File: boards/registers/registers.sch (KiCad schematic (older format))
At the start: 44 parts, among them U1 SN74LV08APW, U2 MC74HC244ADT, U3 MC74HC273ADT, U4 74HC161PW

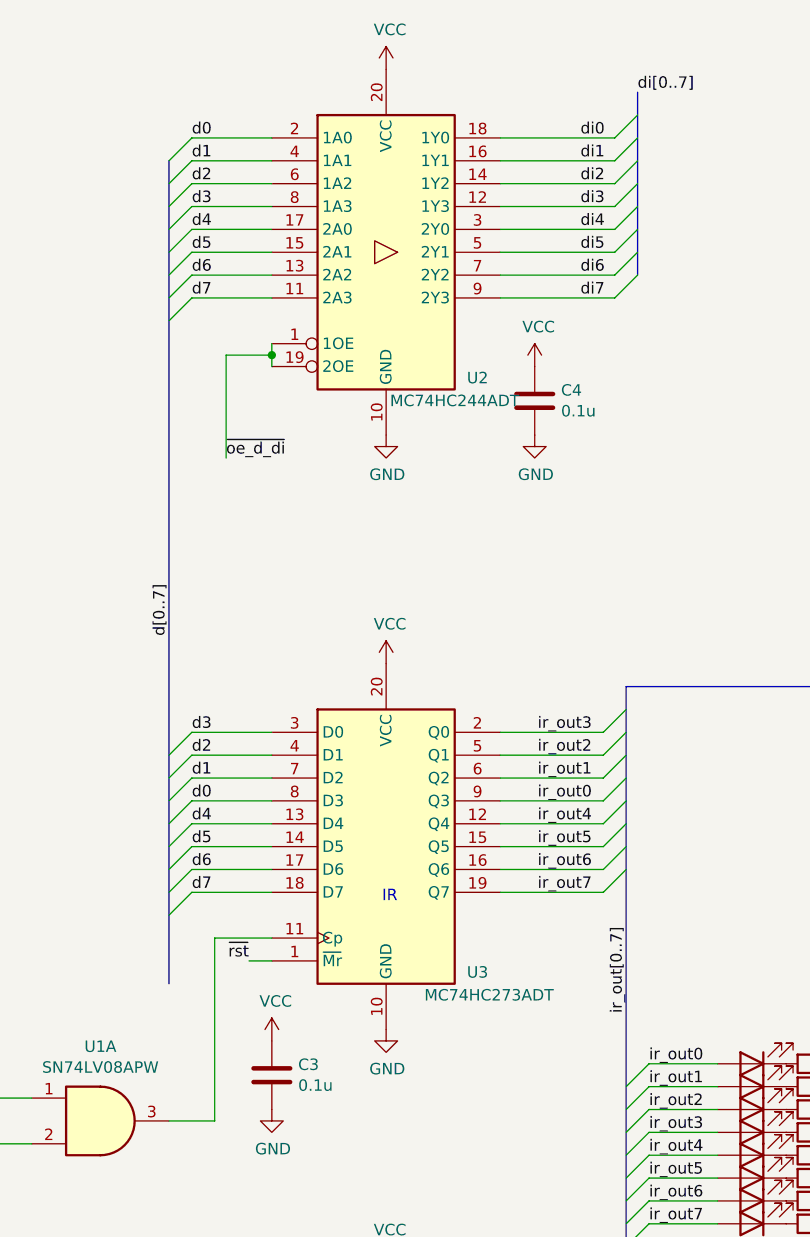
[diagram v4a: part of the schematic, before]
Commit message: Registers board rev. 2
Implement RDY mechanism by suspending clock signal
Take caution against crosstalk on sensitive line
Add proper decoupling capacitors
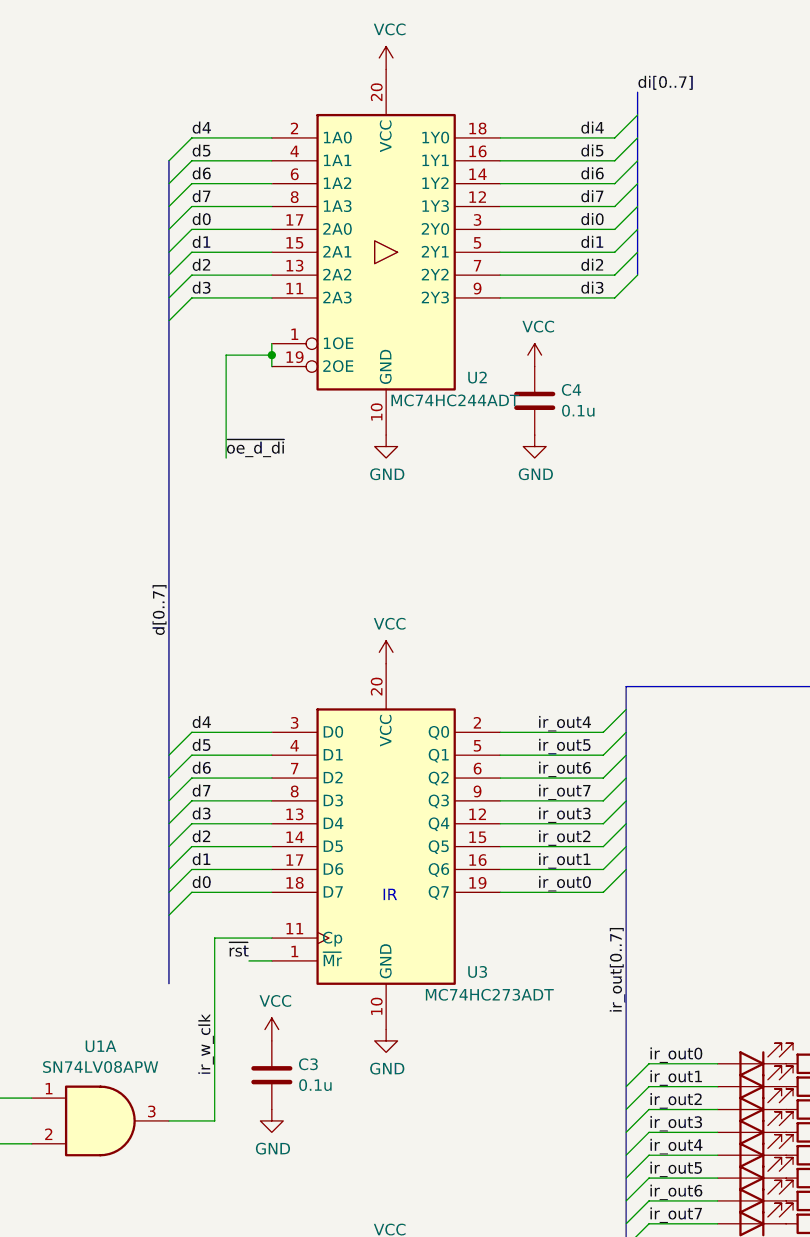
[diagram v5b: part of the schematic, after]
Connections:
- net alu_invert: now also U3.15 (Q5); no longer U3.5 (Q1)
- net alu_op0: now also U3.12 (Q4); no longer U3.2 (Q0)
- net alu_op1: now also U3.2 (Q0); no longer U3.12 (Q4)
- net alu_op2: now also U3.5 (Q1); no longer U3.15 (Q5)
- net alu_op3: now also U3.6 (Q2); no longer U3.16 (Q6)
- net d0: now also U2.17 (2A0), U3.18 (D7); no longer U2.2 (1A0), U3.8 (D3)
- net d1: now also U2.15 (2A1), U3.17 (D6); no longer U2.4 (1A1), U3.7 (D2)
- net d2: now also U2.13 (2A2), U3.14 (D5); no longer U2.6 (1A2), U3.4 (D1)
- net d3: now also U2.11 (2A3), U3.13 (D4); no longer U2.8 (1A3), U3.3 (D0)
- net d4: now also U2.2 (1A0), U3.3 (D0); no longer U2.17 (2A0), U3.13 (D4)
- net d5: now also U2.4 (1A1), U3.4 (D1); no longer U2.15 (2A1), U3.14 (D5)
- net d6: now also U2.6 (1A2), U3.7 (D2); no longer U2.13 (2A2), U3.17 (D6)
- net d7: now also U2.8 (1A3), U3.8 (D3); no longer U2.11 (2A3), U3.18 (D7)
- net di0: now also U2.3 (2Y0); no longer U2.18 (1Y0)
- net di1: now also U2.5 (2Y1); no longer U2.16 (1Y1)
- net di2: now also U2.7 (2Y2); no longer U2.14 (1Y2)
- net di3: now also U2.9 (2Y3); no longer U2.12 (1Y3)
- net di4: now also U2.18 (1Y0); no longer U2.3 (2Y0)
- net di5: now also U2.16 (1Y1); no longer U2.5 (2Y1)
- net di6: now also U2.14 (1Y2); no longer U2.7 (2Y2)
- net di7: now also U2.12 (1Y3); no longer U2.9 (2Y3)
- net ir_out0: now also U3.19 (Q7); no longer U3.9 (Q3)
- net ir_out1: now also U3.16 (Q6); no longer U3.6 (Q2)
- net ir_out7: now also U3.9 (Q3); no longer U3.19 (Q7)
- net ir_w_clk: now reaches U1.3, U3.11 (Cp)
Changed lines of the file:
@@
 ir_out[0..7]
 Wire Wire Line
+	3850 4050 4300 4050
+Wire Wire Line
+	3850 4150 4300 4150
+Wire Wire Line
+	3850 4250 4300 4250
+Wire Wire Line
+	3850 4350 4300 4350
+Wire Wire Line
 	3850 3650 4300 3650
 Wire Wire Line
@@
 Wire Wire Line
 	3850 3950 4300 3950
-Wire Wire Line
-	3850 4050 4300 4050
-Wire Wire Line
-	3850 4150 4300 4150
-Wire Wire Line
-	3850 4250 4300 4250
-Wire Wire Line
-	3850 4350 4300 4350
+Text Label 4250 4050 2    50   ~ 0
+ir_out3
+Text Label 4250 4150 2    50   ~ 0
+ir_out2
+Text Label 4250 4250 2    50   ~ 0
+ir_out1
+Text Label 4250 4350 2    50   ~ 0
+ir_out0
 Text Label 4250 3650 2    50   ~ 0
-ir_out3
+ir_out4
 Text Label 4250 3750 2    50   ~ 0
-ir_out2
+ir_out5
 Text Label 4250 3850 2    50   ~ 0
-ir_out1
+ir_out6
 Text Label 4250 3950 2    50   ~ 0
-ir_out0
-Text Label 4250 4050 2    50   ~ 0
-ir_out4
-Text Label 4250 4150 2    50   ~ 0
-ir_out5
-Text Label 4250 4250 2    50   ~ 0
-ir_out6
-Text Label 4250 4350 2    50   ~ 0
 ir_out7
 Entry Wire Line
@@
 ~clk
 Entry Wire Line
+	2400 1550 2500 1450
+Entry Wire Line
+	2400 1650 2500 1550
+Entry Wire Line
+	2400 1750 2500 1650
+Entry Wire Line
+	2400 1850 2500 1750
+Entry Wire Line
 	2400 1150 2500 1050
 Entry Wire Line
@@
 	2400 1450 2500 1350
 Entry Wire Line
-	2400 1550 2500 1450
-Entry Wire Line
-	2400 1650 2500 1550
-Entry Wire Line
-	2400 1750 2500 1650
-Entry Wire Line
-	2400 1850 2500 1750
-Entry Wire Line
 	2400 3750 2500 3650
 Entry Wire Line
@@
 	2400 4450 2500 4350
 Wire Wire Line
+	2850 3950 2500 3950
+Wire Wire Line
+	2500 3850 2850 3850
+Wire Wire Line
+	2850 3750 2500 3750
+Wire Wire Line
+	2500 3650 2850 3650
+Wire Wire Line
 	2850 4350 2500 4350
 Wire Wire Line
@@
 	2500 4050 2850 4050
 Wire Wire Line
-	2850 3950 2500 3950
-Wire Wire Line
-	2500 3850 2850 3850
-Wire Wire Line
-	2850 3750 2500 3750
-Wire Wire Line
-	2500 3650 2850 3650
+	2500 1450 2850 1450
+Wire Wire Line
+	2850 1550 2500 1550
+Wire Wire Line
+	2500 1650 2850 1650
+Wire Wire Line
+	2850 1750 2500 1750
 Wire Wire Line
 	2500 1050 2850 1050
@@
 Wire Wire Line
 	2850 1350 2500 1350
-Wire Wire Line
-	2500 1450 2850 1450
-Wire Wire Line
-	2850 1550 2500 1550
-Wire Wire Line
-	2500 1650 2850 1650
-Wire Wire Line
-	2850 1750 2500 1750
 Wire Wire Line
 	2850 1950 2850 2000
 Text Label 2400 3000 3    50   ~ 0
 d[0..7]
+Text Label 2500 1450 0    50   ~ 0
+d0
+Text Label 2500 1550 0    50   ~ 0
+d1
+Text Label 2500 1650 0    50   ~ 0
+d2
+Text Label 2500 1750 0    50   ~ 0
+d3
 Text Label 2500 1050 0    50   ~ 0
+d4
+Text Label 2500 1150 0    50   ~ 0
+d5
+Text Label 2500 1250 0    50   ~ 0
+d6
+Text Label 2500 1350 0    50   ~ 0
+d7
+Text Label 2500 4050 0    50   ~ 0
+d3
+Text Label 2500 4150 0    50   ~ 0
+d2
+Text Label 2500 4250 0    50   ~ 0
+d1
+Text Label 2500 4350 0    50   ~ 0
 d0
-Text Label 2500 1150 0    50   ~ 0
-d1
-Text Label 2500 1250 0    50   ~ 0
-d2
-Text Label 2500 1350 0    50   ~ 0
-d3
-Text Label 2500 1450 0    50   ~ 0
+Text Label 2500 3650 0    50   ~ 0
 d4
-Text Label 2500 1550 0    50   ~ 0
+Text Label 2500 3750 0    50   ~ 0
 d5
-Text Label 2500 1650 0    50   ~ 0
+Text Label 2500 3850 0    50   ~ 0
 d6
-Text Label 2500 1750 0    50   ~ 0
+Text Label 2500 3950 0    50   ~ 0
 d7
-Text Label 2500 3650 0    50   ~ 0
-d3
-Text Label 2500 3750 0    50   ~ 0
-d2
-Text Label 2500 3850 0    50   ~ 0
-d1
-Text Label 2500 3950 0    50   ~ 0
-d0
-Text Label 2500 4050 0    50   ~ 0
-d4
-Text Label 2500 4150 0    50   ~ 0
-d5
-Text Label 2500 4250 0    50   ~ 0
-d6
-Text Label 2500 4350 0    50   ~ 0
-d7
-Entry Wire Line
-	4350 1050 4450 950
-Entry Wire Line
-	4350 1150 4450 1050
-Entry Wire Line
-	4350 1250 4450 1150
-Entry Wire Line
-	4350 1350 4450 1250
-Entry Wire Line
-	4350 1450 4450 1350
 Entry Wire Line
 	4350 1550 4450 1450
@@
 di[0..7]
 Text Label 4200 1050 0    50   ~ 0
-di0
+di4
 Text Label 4200 1150 0    50   ~ 0
-di1
+di5
 Text Label 4200 1250 0    50   ~ 0
-di2
+di6
 Text Label 4200 1350 0    50   ~ 0
-di3
-Text Label 4200 1450 0    50   ~ 0
-di4
-Text Label 4200 1550 0    50   ~ 0
-di5
-Text Label 4200 1650 0    50   ~ 0
-di6
-Text Label 4200 1750 0    50   ~ 0
 di7
 Wire Wire Line
@@
 Wire Wire Line
 	3850 1350 4350 1350
-Wire Wire Line
-	3850 1450 4350 1450
-Wire Wire Line
-	3850 1550 4350 1550
-Wire Wire Line
-	3850 1650 4350 1650
-Wire Wire Line
-	3850 1750 4350 1750
 $Comp
 L 74xx:74LS161 U4
@@
 Wire Wire Line
 	2350 10600 2350 10700
+Wire Wire Line
+	3850 1750 4350 1750
+Wire Wire Line
+	3850 1650 4350 1650
+Wire Wire Line
+	3850 1550 4350 1550
+Wire Wire Line
+	3850 1450 4350 1450
+Text Label 4200 1750 0    50   ~ 0
+di3
+Text Label 4200 1650 0    50   ~ 0
+di2
+Text Label 4200 1550 0    50   ~ 0
+di1
+Text Label 4200 1450 0    50   ~ 0
+di0
+Entry Wire Line
+	4350 1450 4450 1350
+Entry Wire Line
+	4350 1350 4450 1250
+Entry Wire Line
+	4350 1250 4450 1150
+Entry Wire Line
+	4350 1150 4450 1050
+Entry Wire Line
+	4350 1050 4450 950
+Text Label 2600 5150 1    50   ~ 0
+ir_w_clk
 Wire Bus Line
 	13750 4550 13750 5950
